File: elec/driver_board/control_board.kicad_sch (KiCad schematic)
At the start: 13 parts, among them J25 button_shutdown, J26 button_mode, J27 rotary_encoder, J28 DCF77 board, J29 RTC, U1 ESP32-C3-DEVKITM-1

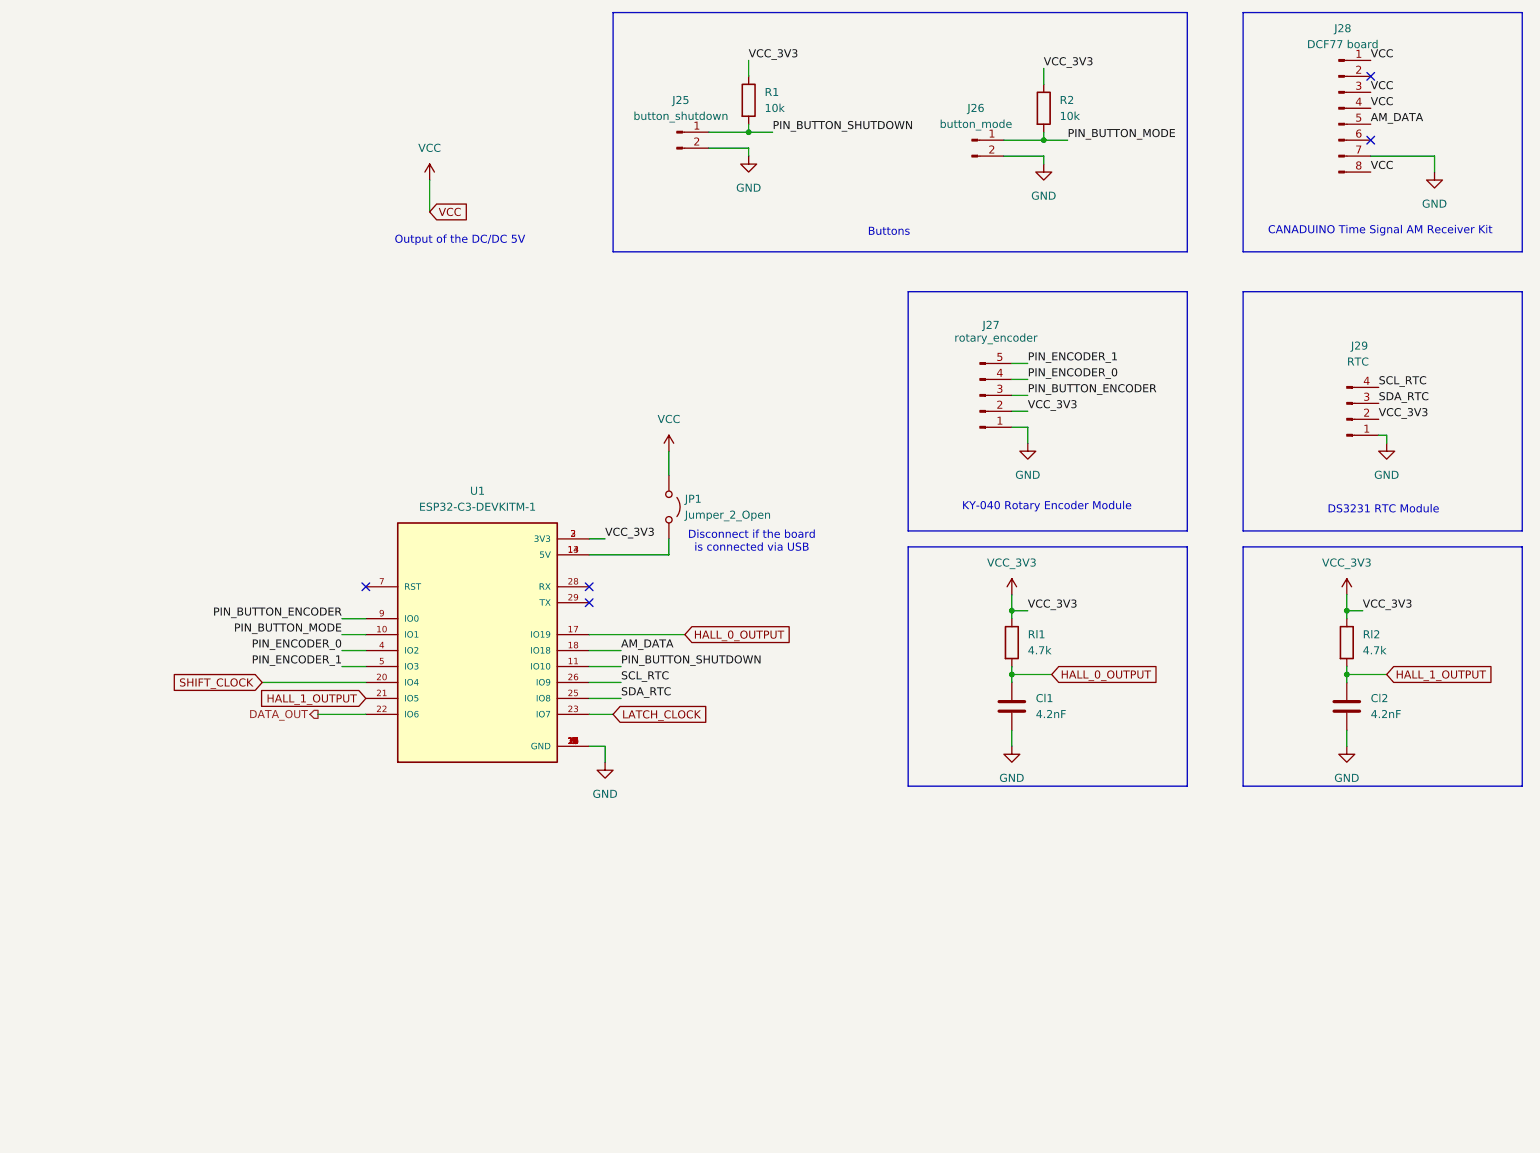
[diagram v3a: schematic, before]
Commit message: [elec] Add space for physical button
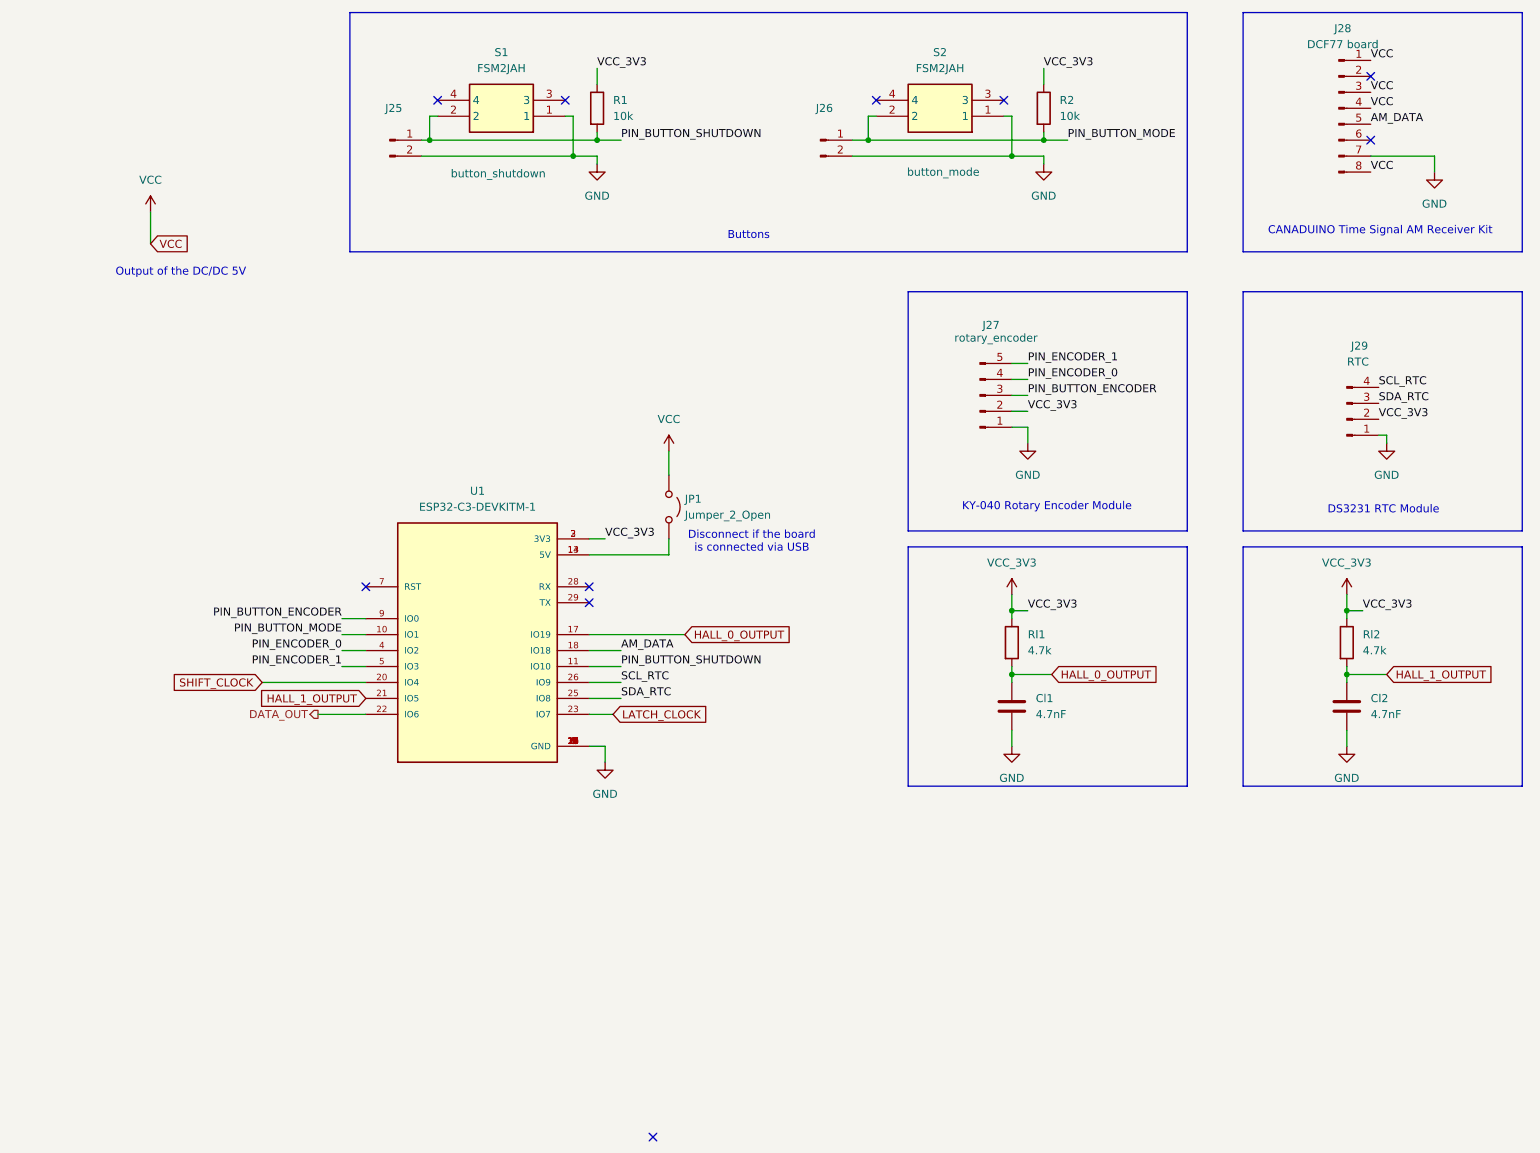
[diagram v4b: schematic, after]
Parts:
- added S1, S2: FSM2JAH, Samacsys:FSM4JH, symbol Samacsys:FSM2JAH
- Cl1, Cl2: value 4.2nF -> 4.7nF
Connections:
- net GND: now also S1.1, S2.1
- net PIN_BUTTON_MODE: now also S2.2
- net PIN_BUTTON_SHUTDOWN: now also S1.2
- no-connect marks 5 -> 10
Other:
- moved on the sheet: J25, J26, R1

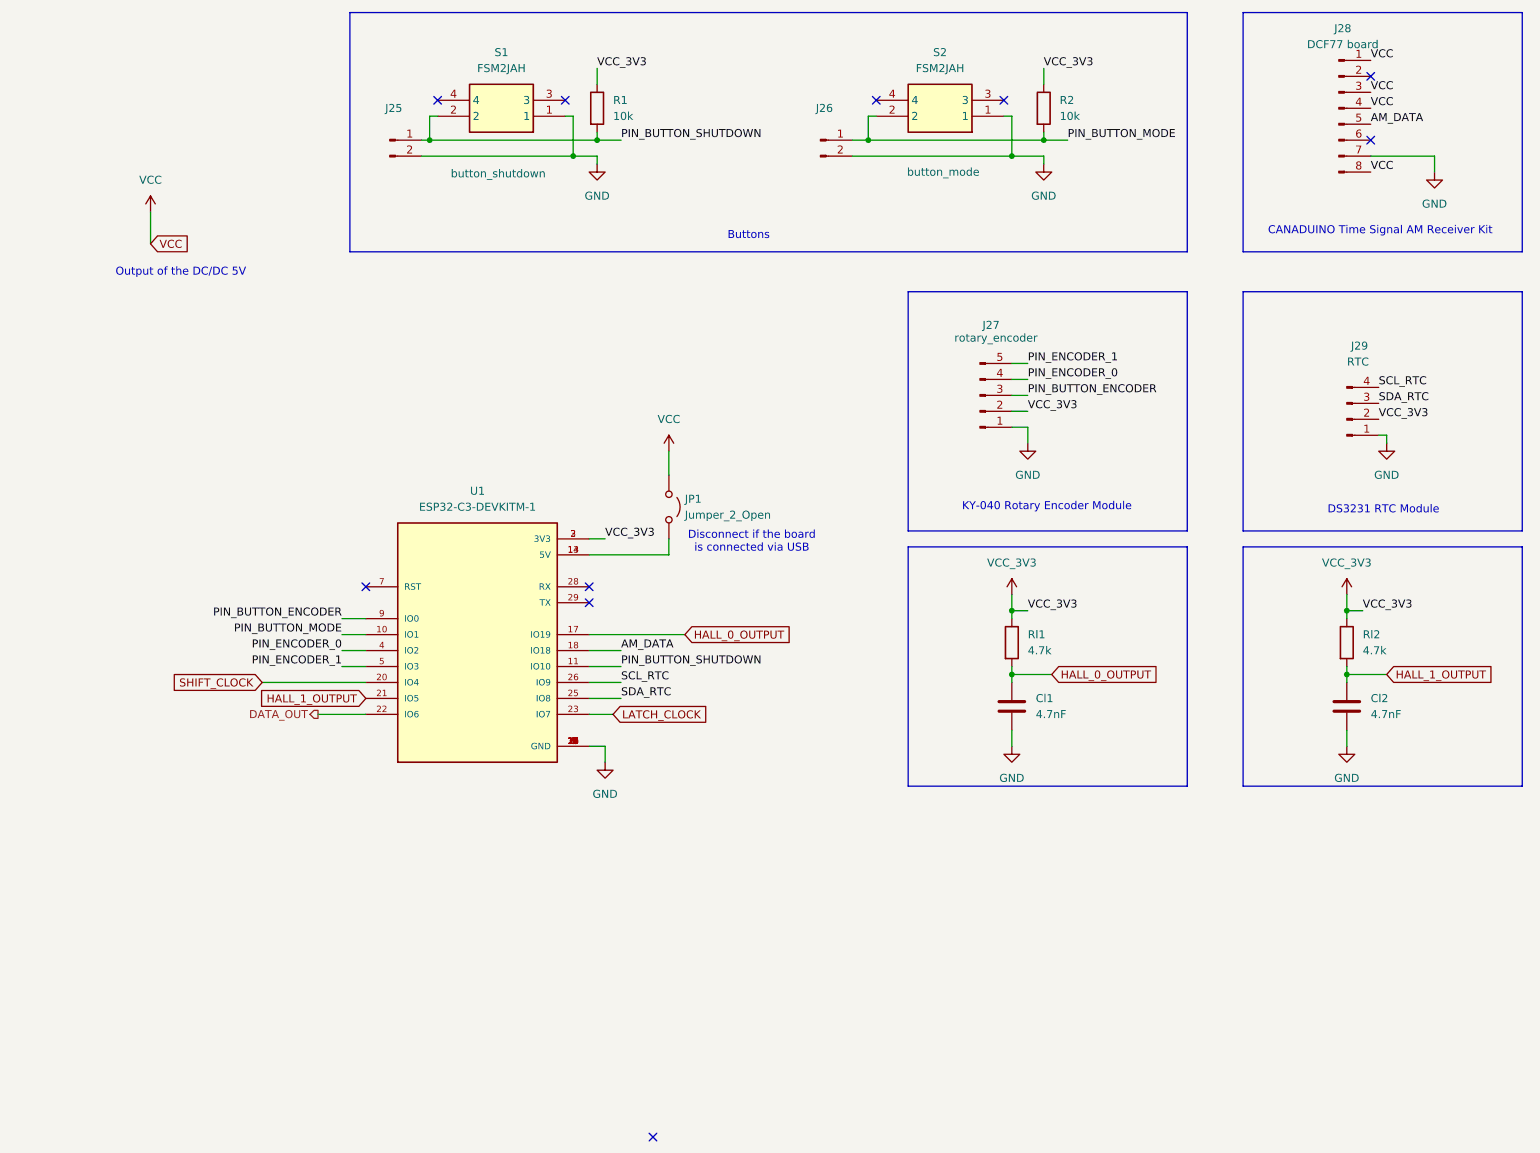
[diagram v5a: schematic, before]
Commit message: Update schematic with VID6606
Use the 'official' driver of VID28-05 motors.
Put back the 74HCT595 bit shift register to link all
motor drivers.
Work in progress.
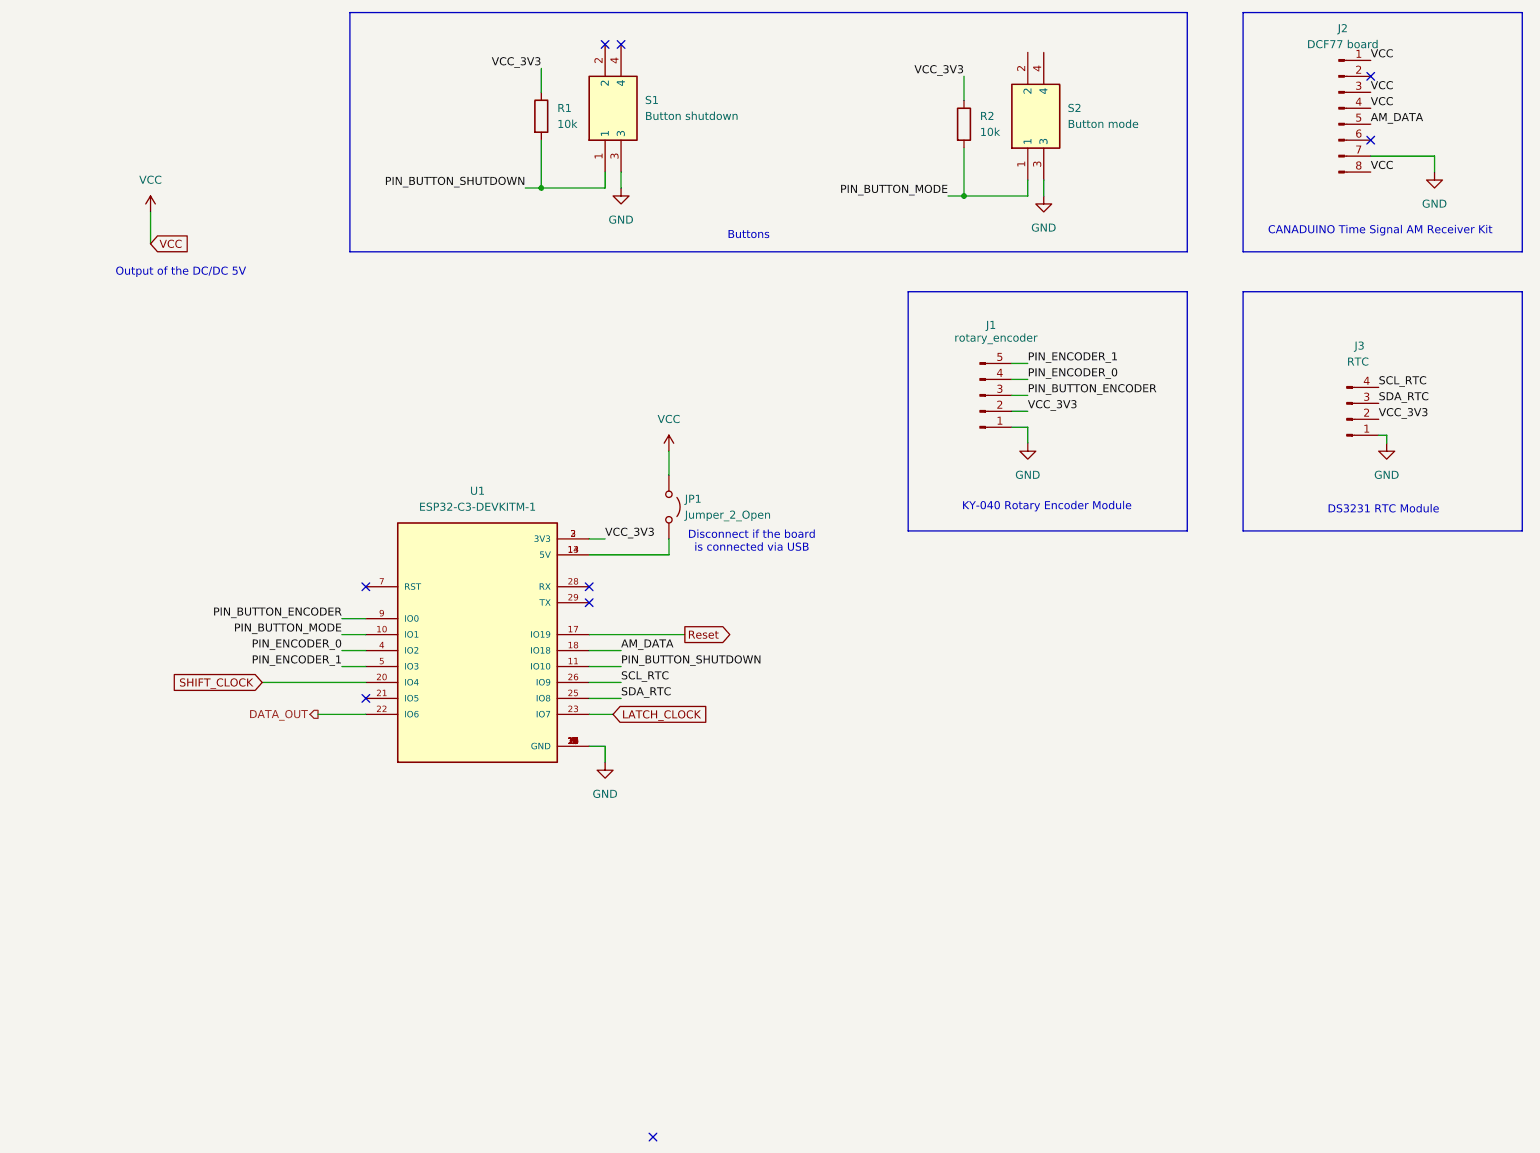
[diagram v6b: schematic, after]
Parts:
- removed Cl1, Cl2: 4.7nF, Capacitor_SMD:C_1206_3216Metric, symbol Device:C
- removed J25: button_shutdown, Connector_PinHeader_2.54mm:PinHeader_1x02_P2.54mm_Vertical, symbol Connector:Conn_01x02_Pin
- removed J26: button_mode, Connector_PinHeader_2.54mm:PinHeader_1x02_P2.54mm_Vertical, symbol Connector:Conn_01x02_Pin
- removed Rl1, Rl2: 4.7k, Capacitor_SMD:C_1206_3216Metric, symbol Device:R
- S1: value FSM2JAH -> Button shutdown
- S2: value FSM2JAH -> Button mode
- renumbered J27 to J1, J28 to J2, J29 to J3
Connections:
- net GND: now also S1.3, S2.3; no longer S1.1, S2.1
- net PIN_BUTTON_MODE: now also S2.1; no longer S2.2
- net PIN_BUTTON_SHUTDOWN: now also S1.1; no longer S1.2
- net HALL_0_OUTPUT renamed Reset
- net HALL_1_OUTPUT: no longer names the net of U1.21 (IO5)
- no-connect marks 10 -> 9

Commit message: New schematic + route
The new design schematic is done.
Route is ongoing
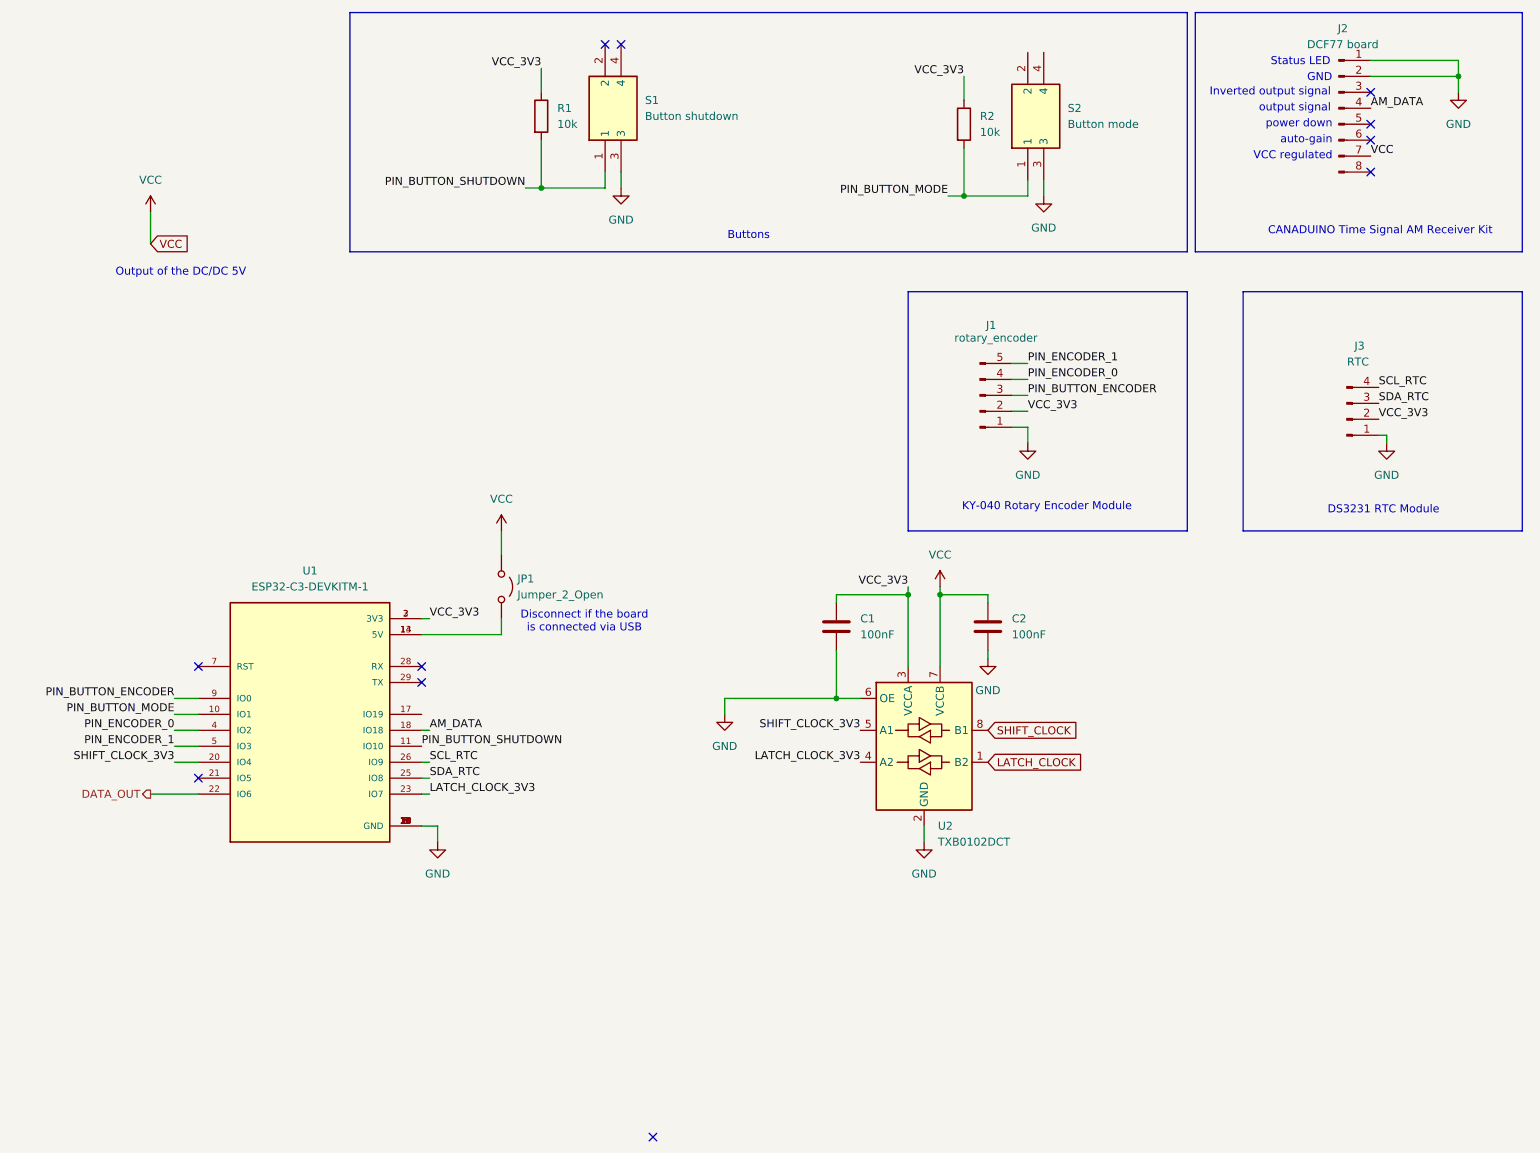
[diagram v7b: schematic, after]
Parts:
- added C1, C2: 100nF, Capacitor_SMD:C_0805_2012Metric, symbol Device:C
- added U2: TXB0102DCT, Package_SO:TSSOP-8_3x3mm_P0.65mm, symbol Logic_LevelTranslator:TXB0102DCT
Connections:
- net AM_DATA: now also J2.4 (Pin_4); no longer J2.5 (Pin_5)
- net GND: now also J2.1 (Pin_1), J2.2 (Pin_2), C1.2, C2.2, U2.2 (GND), U2.6 (OE); no longer J2.7 (Pin_7)
- net LATCH_CLOCK: now also U2.1 (B2); no longer U1.23 (IO7)
- net SHIFT_CLOCK: now also U2.8 (B1); no longer U1.20 (IO4)
- net VCC: now also J2.7 (Pin_7), C2.1, U2.7 (VCCB); no longer J2.1 (Pin_1), J2.3 (Pin_3), J2.4 (Pin_4), J2.8 (Pin_8)
- net VCC_3V3: now also C1.1, U2.3 (VCCA)
- net Reset: no longer names the net of U1.17 (IO19)
- new net LATCH_CLOCK_3V3: U1.23 (IO7), U2.4 (A2)
- new net SHIFT_CLOCK_3V3: U1.20 (IO4), U2.5 (A1)
- no-connect marks 9 -> 11
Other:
- note added: "GND"
- note added: "Inverted output signal"
- note added: "Status LED"
- note added: "VCC regulated"
- note added: "auto-gain"
- note added: "output signal"
- note added: "power down"
- moved on the sheet: JP1, U1
